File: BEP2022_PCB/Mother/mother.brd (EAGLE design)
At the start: 67.3 x 30.5 mm, 17 parts, among them U1 MCP2562-E/P, X1 JST-XH-03-PIN-LONG-PAD, X2 JST-XH-04-PIN-LONG-PAD, X3 JST-XH-04-PIN-LONG-PAD, X4 JST-XH-03-PIN-LONG-PAD

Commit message: update PCB
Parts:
- added JP1: (no value), pinhead:1X10
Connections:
- new net CS: JP1.2, U$1.D4
- new net DI: JP1.3, U$1.D23
- new net DO: JP1.7, U$1.D19
- new net N$1: JP1.1
- new net N$10: JP1.10
- new net N$8: JP1.8
- new net N$9: JP1.9
- new net SCLK: JP1.5, U$1.D18
- net 3V3: now also JP1.4
- net GND: now also JP1.6
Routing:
- net DI: track 0.00 -> 36.2 mm
- net GND: track 165.3 -> 191.1 mm, vias 46 -> 44
- net SCLK: track 0.00 -> 12.2 mm
- net CS: track 0.00 -> 11.1 mm
- net DO: track 0.00 -> 11.0 mm
- net 3V3: track 126.2 -> 129.5 mm
- removed copper zone on layer 1, net GND
- removed copper zone on layer 16, net GND
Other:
- board size 67.3 x 30.5 mm -> 67.3 x 27.4 mm
- board text removed: "SCL"

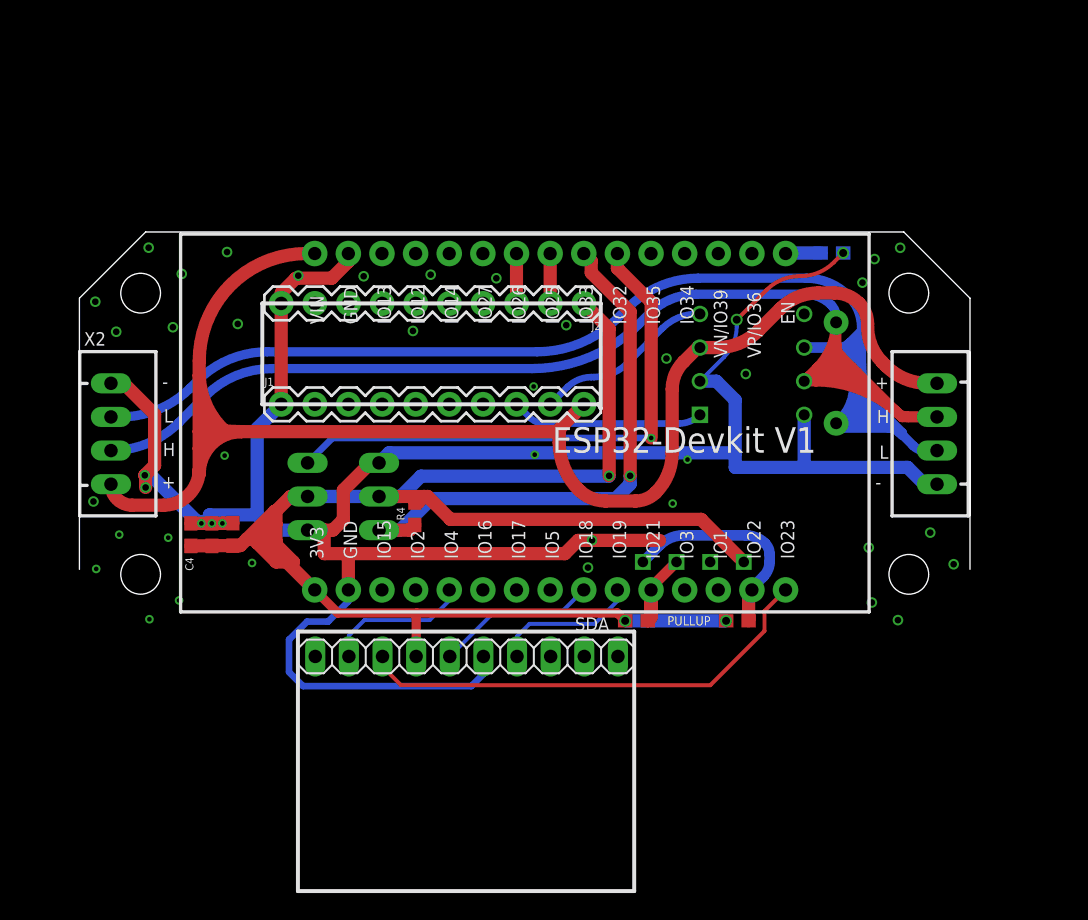
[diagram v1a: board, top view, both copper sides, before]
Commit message: 母機の基板設計をした
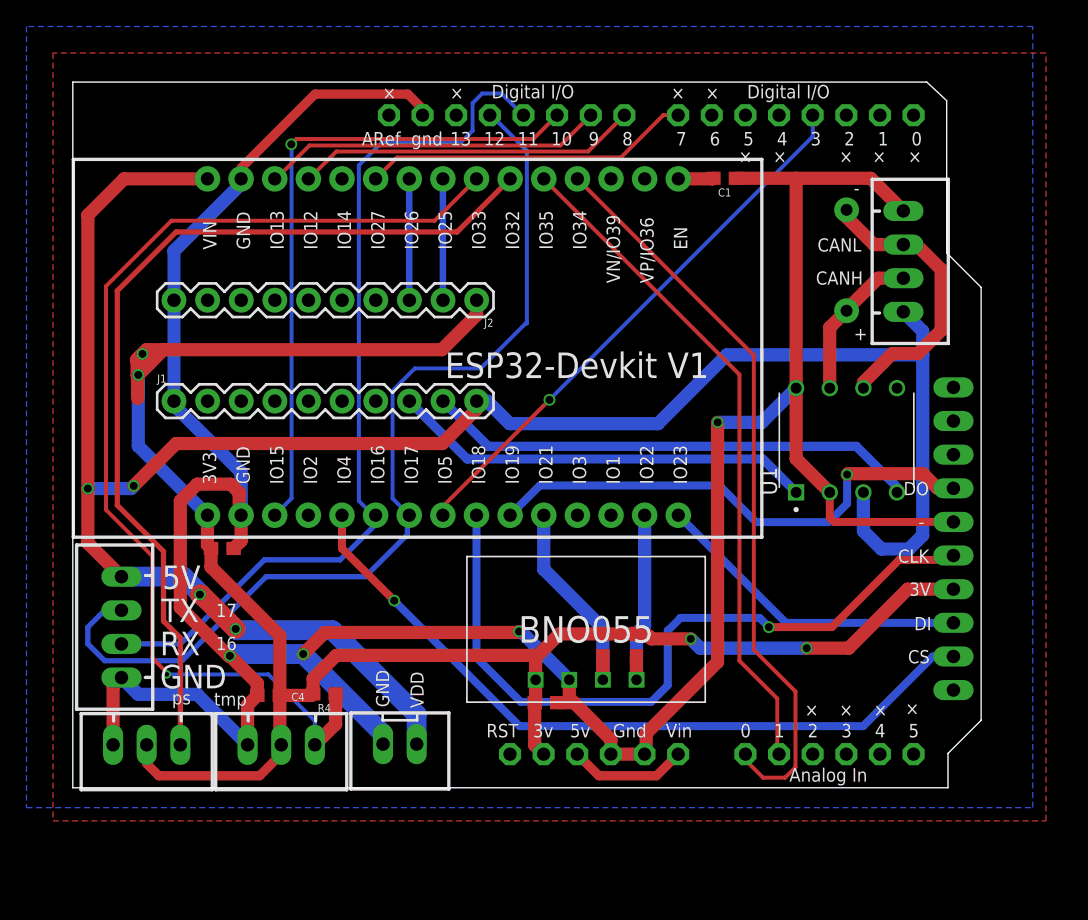
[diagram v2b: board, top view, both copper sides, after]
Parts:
- added U$2: ARDUINO-NOHOLE, adafruit:ARDUINO-NOHOLE
- added X5: JST-XH-04-PIN-LONG-PAD, JST XH Connectors:JST-XH-04-PACKAGE-LONG-PAD
- X2: value JST-XH-04-PIN-LONG-PAD -> JST-XH-02-PIN-LONG-PAD; device JST XH Connectors:JST-XH-04-PACKAGE-LONG-PAD -> JST XH Connectors:JST-XH-02-PACKAGE-LONG-PAD
- moved JP1 37.8 mm to (66.0, 7.31), flipped to the bottom, turned to 90 degrees
- moved X2 32.0 mm to (24.2, -8.20), turned to 180 degrees
- moved C3 26.8 mm to (35.2, -5.07), turned to 0 degrees
- moved X4 22.3 mm to (5.08, -8.26), flipped to the top, turned to 180 degrees
- moved X1 20.2 mm to (15.2, -8.26), flipped to the top, turned to 180 degrees
- moved R4 15.2 mm to (18.5, -4.41), turned to 180 degrees
- moved C4 13.5 mm to (14.3, -4.52), turned to 180 degrees
- moved X3 13.3 mm to (62.2, 28.3), turned to 270 degrees
- moved U$3 12.0 mm to (38.3, 0.47), flipped to the top
- moved C1 9.87 mm to (48.7, 34.5), flipped to the top, turned to 180 degrees
- moved U$1 9.87 mm to (26.2, 21.4)
- moved U1 9.15 mm to (57.9, 14.7), flipped to the top, turned to 90 degrees
- moved R1 8.53 mm to (57.9, 28.3), turned to 270 degrees
- moved J1 8.10 mm to (7.14, 17.7)
- moved J2 8.10 mm to (30.0, 25.3)
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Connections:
- new net GPIO0: U$2.D0
- new net GPIO1: U$1.D1
- new net GPIO12: U$1.D12, U$2.D8
- new net GPIO13: U$1.D13, U$2.D9
- new net GPIO14: U$1.D14
- new net GPIO15: U$1.D15, U$2.D10
- new net GPIO16: U$2.D1
- new net GPIO17: U$2.D2
- new net GPIO18: U$2.D4
- new net GPIO19: U$2.D5
- new net GPIO21: U$2.D6
- new net GPIO25: U$2.A4
- new net GPIO26: U$2.A5
- new net GPIO27: U$1.D27, U$2.D7
- new net GPIO32: U$2.A2
- new net GPIO33: U$2.A3
- new net GPIO34: U$1.D34, U$2.A0
- new net GPIO35: U$1.D35, U$2.A1
- new net GPIO4: U$2.D13
- new net GPIO5: U$1.D5, U$2.D3
- new net N$2: U$1.D3
- new net N$5: U$1.D2
- new net RX: U$1.D16, U$2.D11, X5.2
- new net TX: U$1.D17, U$2.D12, X5.3
- new net VIN: U$2.5V, U$2.VIN
- net 3V3: now also U$2.3V
- net CANH: no longer X2.3
- net CANL: no longer X2.2
- net GND: now also U$2.GND, U$2.GND1, U$2.GND2, X2.2, X5.1; no longer X2.1
- net VDD_5V: now also X2.1, X5.4; no longer X2.4
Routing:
- net TX: track 0.00 -> 95.3 mm
- net CANL: track 114.7 -> 21.9 mm
- net CANH: track 99.6 -> 11.7 mm
- net RX: track 0.00 -> 67.8 mm
- net GPIO34: track 0.00 -> 56.4 mm
- net GPIO35: track 0.00 -> 50.8 mm
- net GPIO15: track 0.00 -> 49.6 mm, vias 0 -> 1
- net CS: track 11.1 -> 56.4 mm, vias 0 -> 1
- net VDD_5V: track 118.3 -> 162.3 mm, vias 0 -> 4
- net SCLK: track 12.2 -> 55.7 mm, vias 0 -> 1
- net GPIO5: track 0.00 -> 41.8 mm, vias 0 -> 1
- net 1WIRE: track 42.1 -> 81.6 mm
- net GND: track 191.1 -> 227.4 mm, vias 44 -> 4
- net DO: track 11.0 -> 38.8 mm, vias 0 -> 1
- net AIN: track 41.7 -> 69.4 mm, vias 1 -> 0
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- added copper zone on layer 1, net GND
- added copper zone on layer 16, net GND
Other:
- board size 67.3 x 27.4 mm -> 68.6 x 53.3 mm
- board text added: "16"
- board text added: "17"
- board text added: "3V"
- board text added: "A"
- board text added: "CANH"
- board text added: "CANL"
- board text added: "CLK"
- board text added: "CS"
- board text added: "DI"
- board text added: "DO"
- board text added: "RX"
- board text added: "TX"
- board text added: "ps"
- board text added: "tmp"
- board text added: "w"
- board text added: "×"
- board text removed: "32"
- board text removed: "33"
- board text removed: "3V3"
- board text removed: "AIN"
- board text removed: "CANRX"
- board text removed: "CANTX"
- board text removed: "CH"
- board text removed: "CL"
- board text removed: "CR"
- board text removed: "CRX_H"
- board text removed: "CT"
- board text removed: "CTX_H"
- board text removed: "H"
- board text removed: "L"
- board text removed: "LoggerV1"
- board text removed: "PULLUP"
- board text removed: "SDA"
- board text removed: "TMP"
- board text removed: "VIN"

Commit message: 基板のアップデート
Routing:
- net GND: vias 4 -> 99
